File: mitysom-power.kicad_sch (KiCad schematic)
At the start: 25 parts, among them J1 Plug_Samtec_SEAM-50-02.0-L-08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, J2 PinHeader_1x3_P2.54mm_Drill1.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

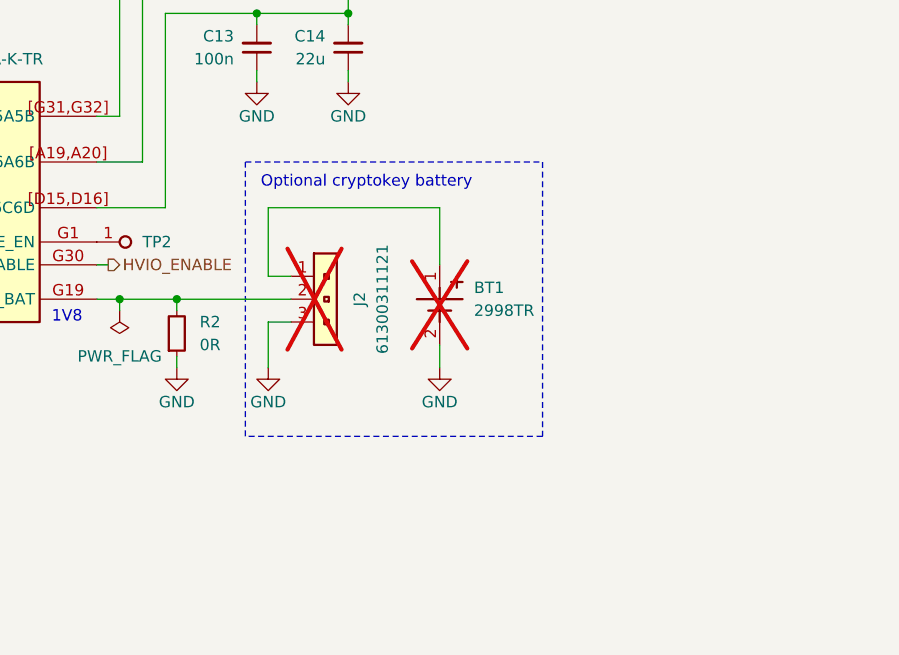
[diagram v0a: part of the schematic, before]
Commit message: [#100687] Replace battery with LDO
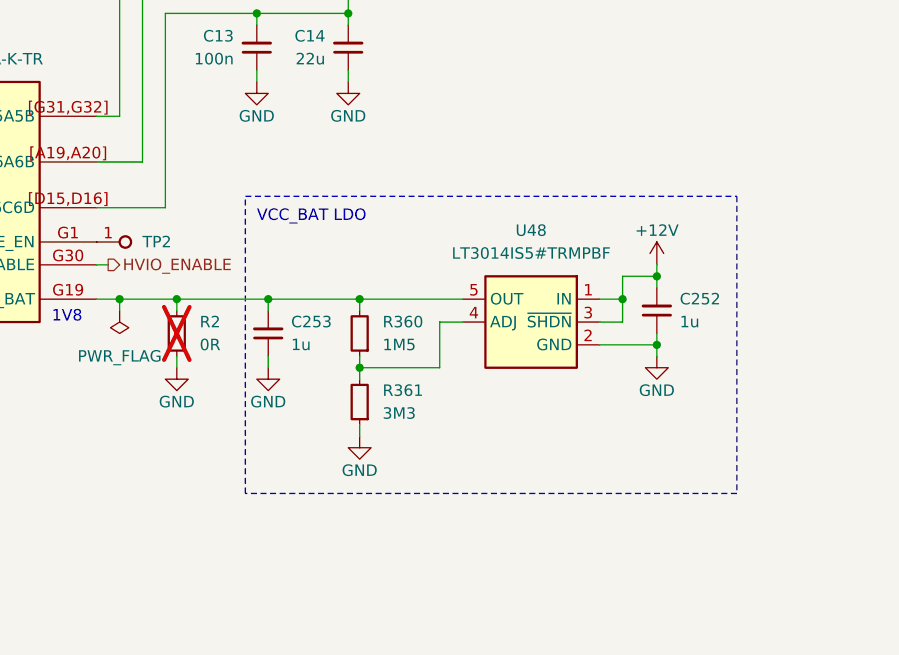
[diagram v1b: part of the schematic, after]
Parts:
- removed BT1: Battery_Holder_2998TR, antmicro-footprints:Battery_Holder_2998TR, symbol antmicroBatteryHoldersClipsContacts:Battery_Holder_2998TR
- removed J2: PinHeader_1x3_P2.54mm_Drill1.1mm, antmicro-footprints:PinHeader_1x3_P2.54mm_Drill1.1mm, symbol antmicroGenericPinHeaders:PinHeader_1x3_P2.54mm_Drill1.1mm
- added C252, C253: C_1u_25V_0402, antmicro-footprints:C_0402_1005Metric, symbol antmicroCapacitors0402:C_1u_25V_0402
- added R360: R_1M5_0402, antmicro-footprints:R_0402_1005Metric, symbol antmicroResistors0402:R_1M5_0402
- added R361: R_3M3_0402, antmicro-footprints:R_0402_1005Metric, symbol antmicroResistors0402:R_3M3_0402
- added U48: LT3014IS5_SOT, antmicro-footprints:SOT-23-5, symbol antmicroPMICVoltageRegulatorsLinear:LT3014IS5_SOT
- R2: now not fitted
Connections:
- net +12V: now also C252.2, U48.1 (IN), U48.3 (~{SHDN})
- net GND: now also C252.1, C253.1, R361.1, U48.2 (GND)
- net at J1.G19 (VCC_BAT), R2.2: now also C253.2, R360.2, U48.5 (OUT)
- new net: R360.1, R361.2, U48.4 (ADJ)
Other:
- note added: "VCC_BAT LDO"
- note removed: "Optional cryptokey battery"

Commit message: [#100687] DNP LDO
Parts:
- C252, C253, R360, R361, U48: now not fitted
- R2: now fitted
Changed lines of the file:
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@@
 		(on_board yes)
 		(in_pos_files yes)
-		(dnp no)
+		(dnp yes)
 		(fields_autoplaced yes)
 		(property "Reference" "U48"
@@
 		(on_board yes)
 		(in_pos_files yes)
-		(dnp no)
+		(dnp yes)
 		(fields_autoplaced yes)
 		(property "Reference" "R360"
@@
 		(on_board yes)
 		(in_pos_files yes)
-		(dnp no)
+		(dnp yes)
 		(fields_autoplaced yes)
 		(property "Reference" "R361"
@@
 		(on_board yes)
 		(in_pos_files yes)
-		(dnp no)
+		(dnp yes)
 		(fields_autoplaced yes)
 		(property "Reference" "C252"
@@
 		(on_board yes)
 		(in_pos_files yes)
-		(dnp yes)
+		(dnp no)
 		(fields_autoplaced yes)
 		(property "Reference" "R2"
@@
 		(on_board yes)
 		(in_pos_files yes)
-		(dnp no)
+		(dnp yes)
 		(fields_autoplaced yes)
 		(property "Reference" "C253"

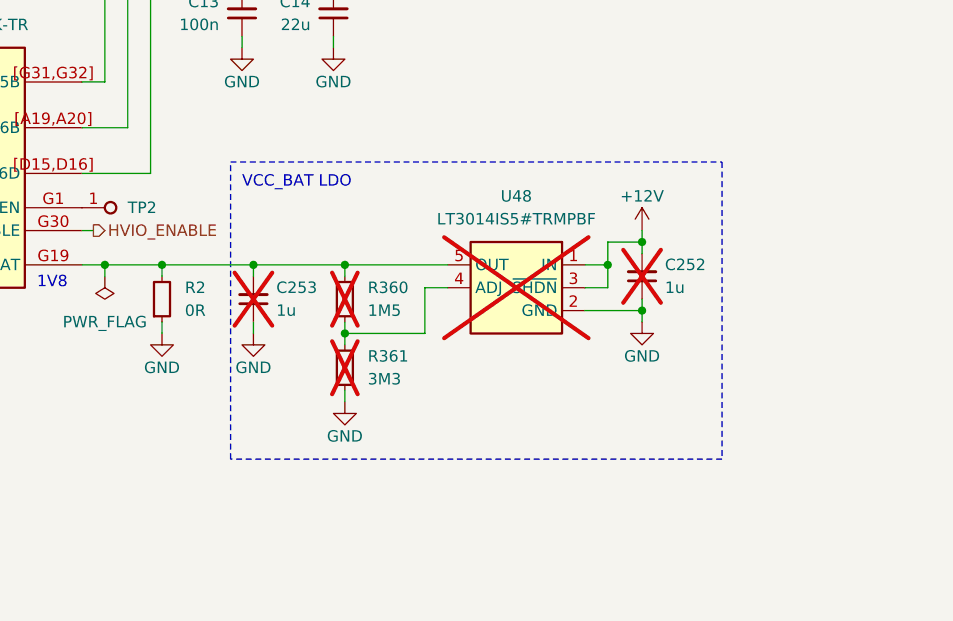
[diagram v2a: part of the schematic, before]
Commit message: [#100687] Update LDO and CLK
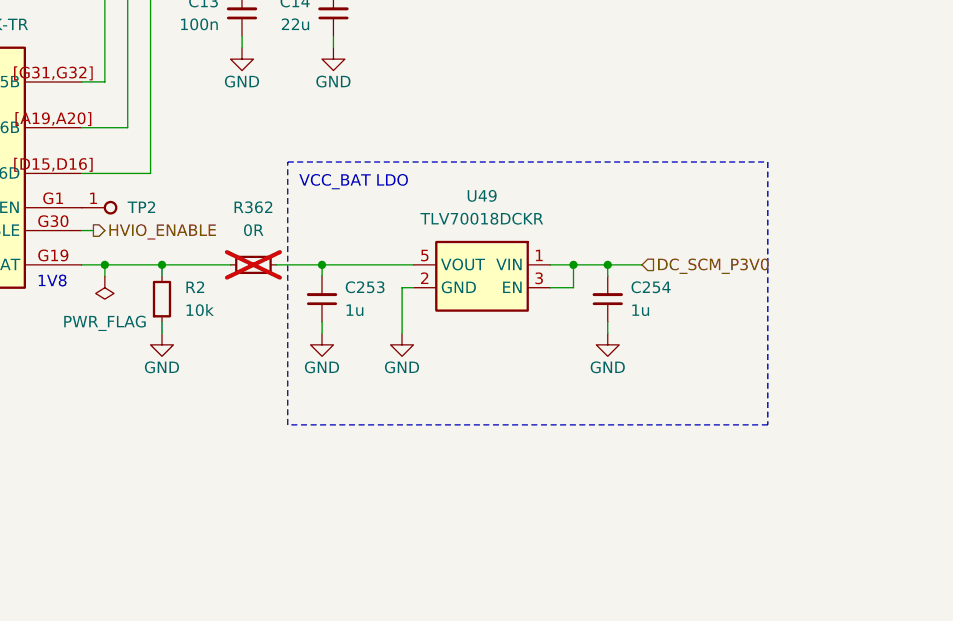
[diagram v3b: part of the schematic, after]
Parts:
- removed C252: C_1u_25V_0402, antmicro-footprints:C_0402_1005Metric, symbol antmicroCapacitors0402:C_1u_25V_0402
- removed R2: R_0R_0402, antmicro-footprints:R_0402_1005Metric, symbol antmicroResistors0402:R_0R_0402
- removed R360: R_1M5_0402, antmicro-footprints:R_0402_1005Metric, symbol antmicroResistors0402:R_1M5_0402
- removed R361: R_3M3_0402, antmicro-footprints:R_0402_1005Metric, symbol antmicroResistors0402:R_3M3_0402
- removed U48: LT3014IS5_SOT, antmicro-footprints:SOT-23-5, symbol antmicroPMICVoltageRegulatorsLinear:LT3014IS5_SOT
- added C254: C_1u_25V_0402, antmicro-footprints:C_0402_1005Metric, symbol antmicroCapacitors0402:C_1u_25V_0402
- added R2: R_10k_0402, antmicro-footprints:R_0402_1005Metric, symbol antmicroResistors0402:R_10k_0402
- added R362: R_0R_0402, antmicro-footprints:R_0402_1005Metric, symbol antmicroResistors0402:R_0R_0402
- added U49: TLV70018_SC70, antmicro-footprints:SC-70-5, symbol antmicroPMICVoltageRegulatorsLinear:TLV70018_SC70
- C253: now fitted
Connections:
- net GND: now also C254.1, R2.1, U49.2 (GND)
- net at C253.2: now also R362.2, U49.5 (VOUT); no longer J1.G19 (VCC_BAT)
- new net: J1.G19 (VCC_BAT), R2.2, R362.1
- new net DC_SCM_P3V0: C254.2, U49.1 (VIN), U49.3 (EN)

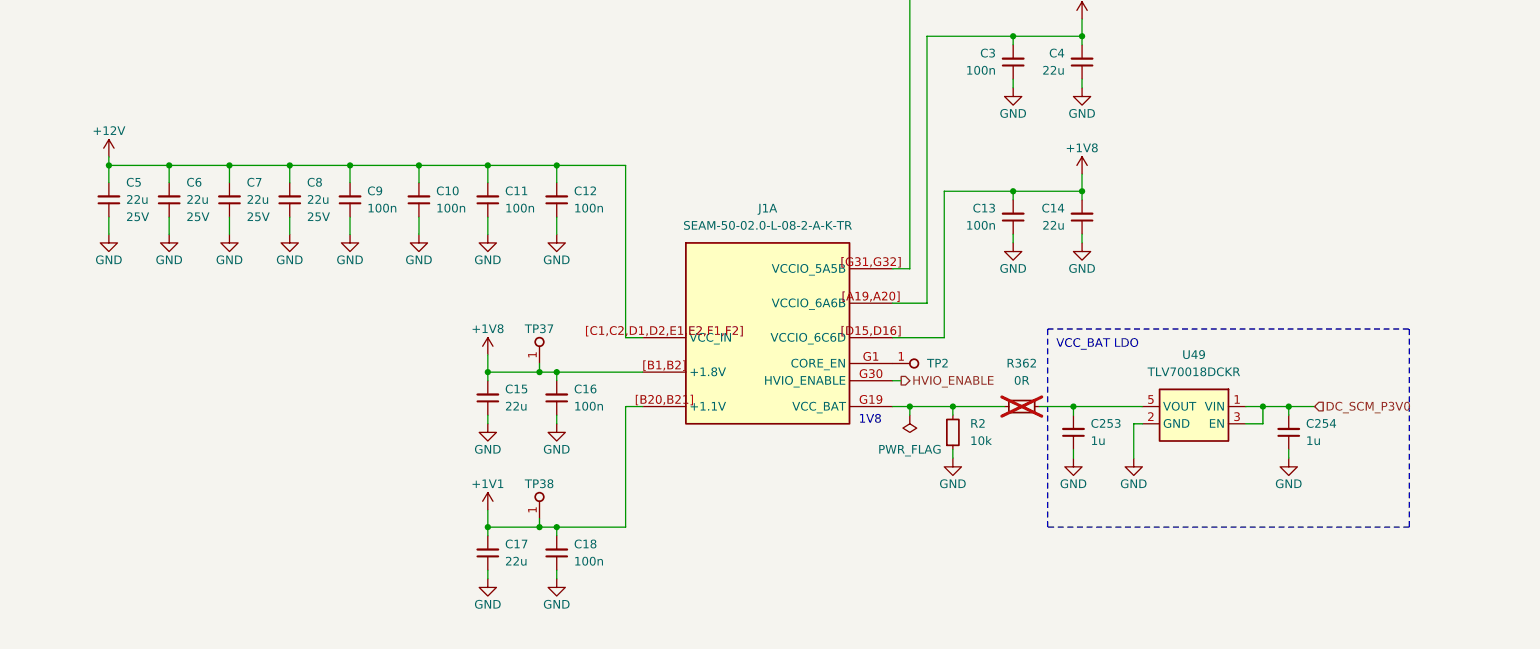
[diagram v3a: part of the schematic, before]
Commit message: [#100687] Update I2C connections
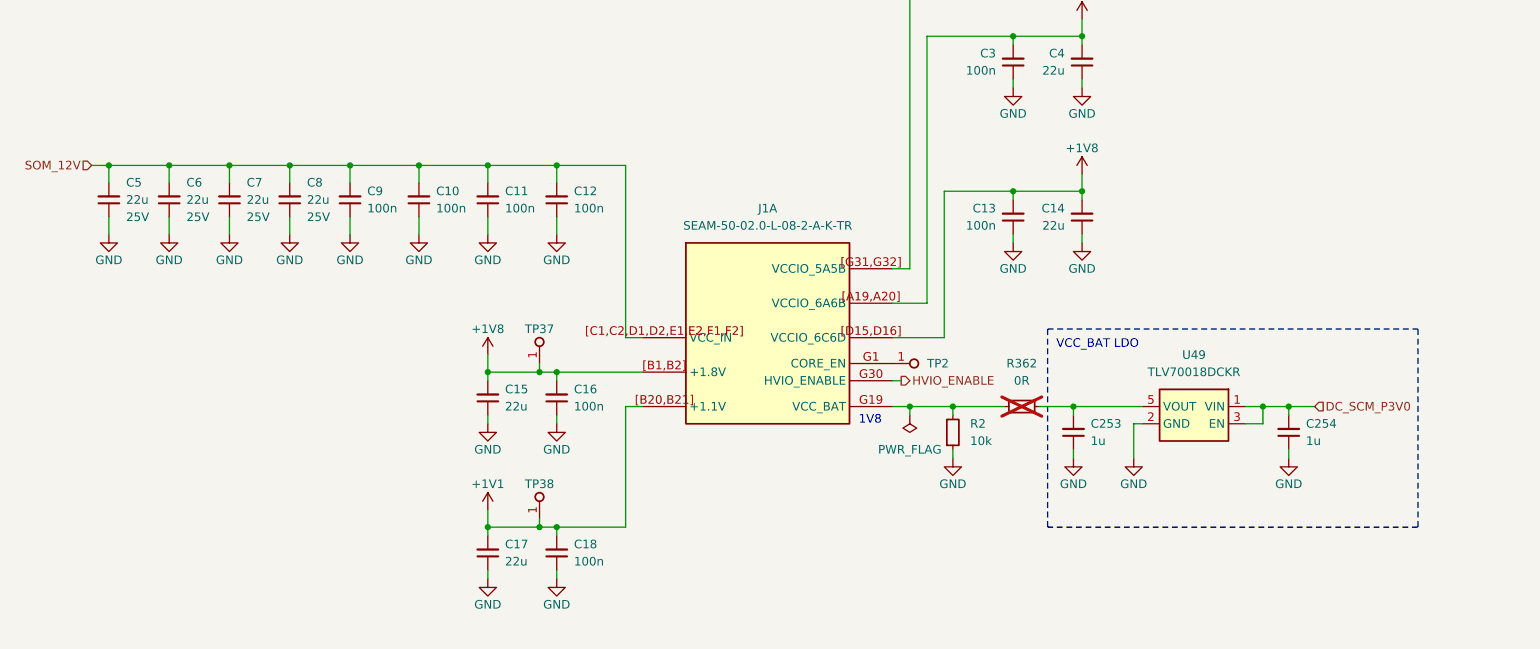
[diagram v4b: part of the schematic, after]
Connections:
- net +12V renamed SOM_12V
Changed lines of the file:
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@@
 	(rectangle
 		(start 193.04 163.83)
-		(end 246.38 193.04)
+		(end 247.65 193.04)
 		(stroke
 			(width 0)
@@
 	(wire
 		(pts
-			(xy 54.61 138.43) (xy 54.61 139.7)
-		)
-		(stroke
-			(width 0)
-			(type default)
-		)
-	)
-	(wire
-		(pts
 			(xy 295.91 162.56) (xy 298.45 162.56)
 		)
@@
 	(wire
 		(pts
+			(xy 52.07 139.7) (xy 54.61 139.7)
+		)
+		(stroke
+			(width 0)
+			(type default)
+		)
+	)
+	(wire
+		(pts
 			(xy 323.85 167.64) (xy 327.66 167.64)
 		)
@@
 		)
 	)
+	(hierarchical_label "SOM_12V"
+		(shape input)
+		(at 52.07 139.7 180)
+		(effects
+			(font
+				(size 1.27 1.27)
+			)
+			(justify right)
+		)
+	)
 	(hierarchical_label "DC_SCM_P3V0"
 		(shape input)
@@
 					(unit 1)
 				)
-			)
-		)
-	)
-	(symbol
-		(lib_id "antmicropower:+12V")
-		(at 54.61 138.43 0)
-		(unit 1)
-		(body_style 1)
-		(exclude_from_sim no)
-		(in_bom yes)
-		(on_board yes)
-		(in_pos_files yes)
-		(dnp no)
-		(property "Reference" "#PWR014"
-			(at 54.61 142.24 0)
-			(hide yes)
-			(show_name no)
-			(do_not_autoplace no)
-			(effects
-				(font
-					(size 1.27 1.27)
-				)
-			)
-		)
-		(property "Value" "+12V"
-			(at 54.61 134.62 0)
-			(show_name no)
-			(do_not_autoplace no)
-			(effects
-				(font
-					(size 1.27 1.27)
-				)
-			)
-		)
-		(property "Footprint" ""
-			(at 54.61 138.43 0)
-			(hide yes)
-			(show_name no)
-			(do_not_autoplace no)
-			(effects
-				(font
-					(size 1.27 1.27)
-				)
-			)
-		)
-		(property "Datasheet" ""
-			(at 54.61 138.43 0)
-			(hide yes)
-			(show_name no)
-			(do_not_autoplace no)
-			(effects
-				(font
-					(size 1.27 1.27)
-				)
-			)
-		)
-		(property "Description" ""
-			(at 54.61 138.43 0)
-			(hide yes)
-			(show_name no)
-			(do_not_autoplace no)
-			(effects
-				(font
-					(size 1.27 1.27)
-				)
-			)
-		)
-		(pin "1"
-		)
-		(instances
-			(project "altera-modular-agilex-5-dc-scm"
-				(path "/6bb9d978-a328-4b30-874b-55170a976185/ccfd355f-9460-404d-be61-24db575a0371"
-					(reference "#PWR014")
-					(unit 1)
-				)
